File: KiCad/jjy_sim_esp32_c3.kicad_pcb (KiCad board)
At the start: 2 copper layers, 50 x 100 mm, 98 parts, among them J1 UART, J2 BAT, M1 NEJI_M3, M2 NEJI_M3, M3 NEJI_M3, M4 NEJI_M3, P1 USB_C_Plug_USB2.0, Q1 BSS84, Q2 2PD601AR, Q3 HN1C01FU-GR (1/2)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

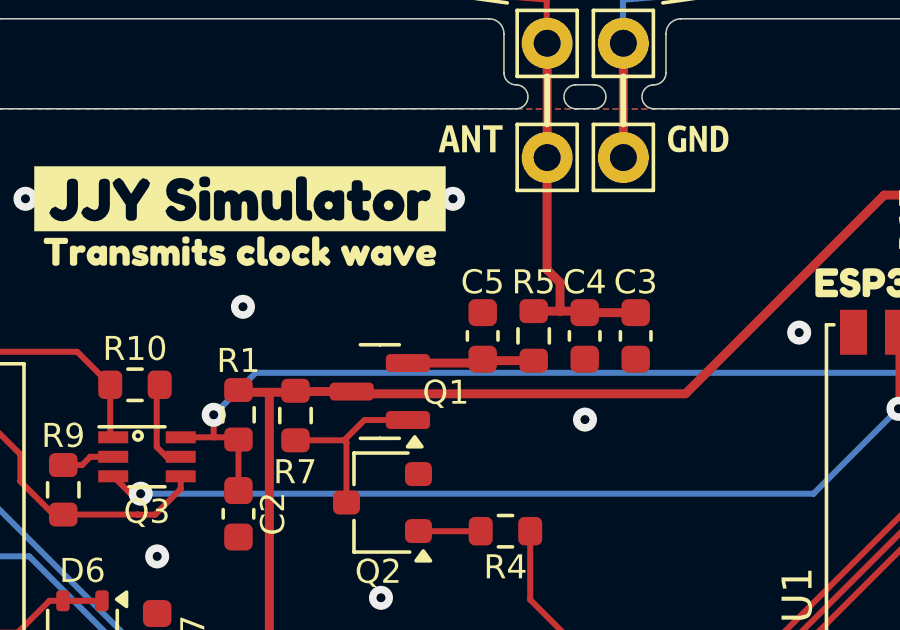
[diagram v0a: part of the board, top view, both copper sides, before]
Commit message: C3,C4定数変更、C5をR18に変更
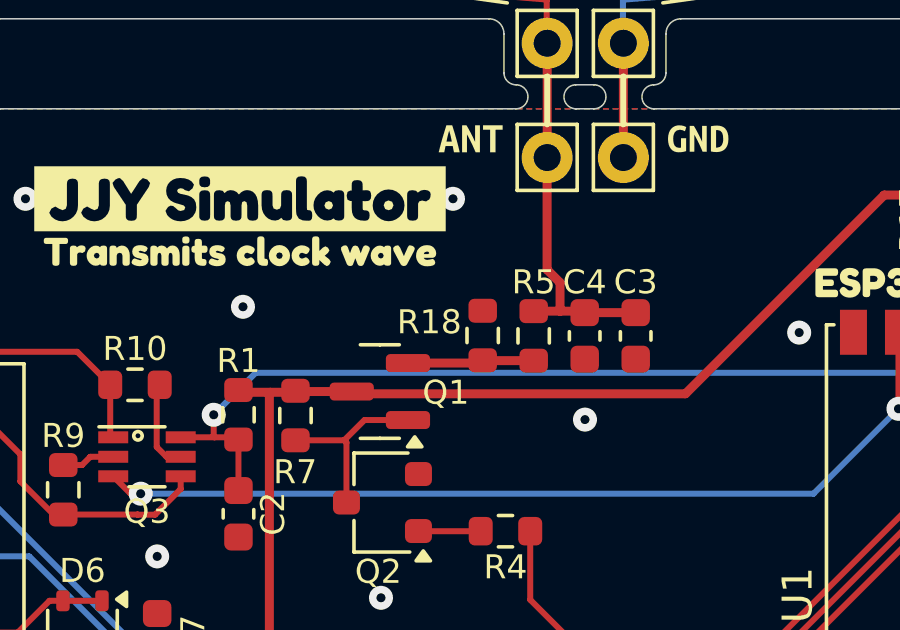
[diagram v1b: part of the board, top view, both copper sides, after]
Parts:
- removed C5: 0.1u, Capacitor_SMD:C_0603_1608Metric
- added R18: 100k, Resistor_SMD:R_0603_1608Metric, F.Cu at (121.6, 107.6)
- C3, C4: value 0.1u -> 1nF
- D2: value LED-IND -> LED-Wave
- D3: value LED-ACT -> LED-WiFi
- D4: value LED-PWR -> LED-Power
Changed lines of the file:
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@@
 			)
 		)
-		(property "Value" "LED-IND"
+		(property "Value" "LED-Wave"
 			(at 0 1.43 180)
 			(layer "F.Fab")
@@
 			)
 		)
-		(property "Value" "0.1u"
+		(property "Value" "1nF"
 			(at 0 1.43 90)
 			(layer "F.Fab")
@@
 		)
 	)
-	(footprint "Capacitor_SMD:C_0603_1608Metric"
-		(layer "F.Cu")
-		(at 121.59 107.57 90)
-		(descr "Capacitor SMD 0603 (1608 Metric), square (rectangular) end terminal, IPC_7351 nominal, (Body size source: IPC-SM-782 page 76, https://www.pcb-3d.com/wordpress/wp-content/uploads/ipc-sm-782a_amendment_1_and_2.pdf), generated with kicad-footprint-generator")
-		(tags "capacitor")
-		(property "Reference" "C5"
-			(at 1.79 0 180)
-			(layer "F.SilkS")
-			(effects
-				(font
-					(size 0.8 0.8)
-					(thickness 0.12)
-				)
-			)
-		)
-		(property "Value" "0.1u"
-			(at 0 1.43 90)
-			(layer "F.Fab")
-			(effects
-				(font
-					(size 0.8 0.8)
-					(thickness 0.12)
-				)
-			)
-		)
-		(property "Footprint" "Capacitor_SMD:C_0603_1608Metric"
-			(at 0 0 90)
-			(unlocked yes)
-			(layer "F.Fab")
-			(hide yes)
-			(effects
-				(font
-					(size 1.27 1.27)
-					(thickness 0.15)
-				)
-			)
-		)
-		(property "Datasheet" ""
-			(at 0 0 90)
-			(unlocked yes)
-			(layer "F.Fab")
-			(hide yes)
-			(effects
-				(font
-					(size 1.27 1.27)
-					(thickness 0.15)
-				)
-			)
-		)
-		(property "Description" ""
-			(at 0 0 90)
-			(unlocked yes)
-			(layer "F.Fab")
-			(hide yes)
-			(effects
-				(font
-					(size 1.27 1.27)
-					(thickness 0.15)
-				)
-			)
-		)
-		(property ki_fp_filters "C_*")
-		(sheetname "ルート")
-		(sheetfile "jjy_sim_esp32_c3.kicad_sch")
-		(attr smd)
-		(fp_line
-			(start -0.14058 -0.51)
-			(end 0.14058 -0.51)
-			(stroke
-				(width 0.12)
-				(type solid)
-			)
-			(layer "F.SilkS")
-		)
-		(fp_line
-			(start -0.14058 0.51)
-			(end 0.14058 0.51)
-			(stroke
-				(width 0.12)
-				(type solid)
-			)
-			(layer "F.SilkS")
-		)
-		(fp_line
-			(start 1.48 -0.73)
-			(end 1.48 0.73)
-			(stroke
-				(width 0.05)
-				(type solid)
-			)
-			(layer "F.CrtYd")
-		)
-		(fp_line
-			(start -1.48 -0.73)
-			(end 1.48 -0.73)
-			(stroke
-				(width 0.05)
-				(type solid)
-			)
-			(layer "F.CrtYd")
-		)
-		(fp_line
-			(start 1.48 0.73)
-			(end -1.48 0.73)
-			(stroke
-				(width 0.05)
-				(type solid)
-			)
-			(layer "F.CrtYd")
-		)
-		(fp_line
-			(start -1.48 0.73)
-			(end -1.48 -0.73)
-			(stroke
-				(width 0.05)
-				(type solid)
-			)
-			(layer "F.CrtYd")
-		)
-		(fp_line
-			(start 0.8 -0.4)
-			(end 0.8 0.4)
-			(stroke
-				(width 0.1)
-				(type solid)
-			)
-			(layer "F.Fab")
-		)
-		(fp_line
-			(start -0.8 -0.4)
-			(end 0.8 -0.4)
-			(stroke
-				(width 0.1)
-				(type solid)
-			)
-			(layer "F.Fab")
-		)
-		(fp_line
-			(start 0.8 0.4)
-			(end -0.8 0.4)
-			(stroke
-				(width 0.1)
-				(type solid)
-			)
-			(layer "F.Fab")
-		)
-		(fp_line
-			(start -0.8 0.4)
-			(end -0.8 -0.4)
-			(stroke
-				(width 0.1)
-				(type solid)
-			)
-			(layer "F.Fab")
-		)
-		(fp_text user "${REFERENCE}"
-			(at 0 0 90)
-			(layer "F.Fab")
-			(effects
-				(font
-					(size 0.4 0.4)
-					(thickness 0.06)
-				)
-			)
-		)
-		(pad "1" smd roundrect
-			(at -0.775 0 90)
-			(size 0.9 0.95)
-			(layers "F.Cu" "F.Paste" "F.Mask")
-			(roundrect_rratio 0.25)
-			(net 5 "Net-(Q1-S)")
-			(pintype "passive")
-		)
-		(pad "2" smd roundrect
-			(at 0.775 0 90)
-			(size 0.9 0.95)
-			(layers "F.Cu" "F.Paste" "F.Mask")
-			(roundrect_rratio 0.25)
-			(net 1 "GND")
-			(pintype "passive")
-		)
-		(model "${KICAD8_3DMODEL_DIR}/Capacitor_SMD.3dshapes/C_0603_1608Metric.wrl"
-			(offset
-				(xyz 0 0 0)
-			)
-			(scale
-				(xyz 1 1 1)
-			)
-			(rotate
-				(xyz 0 0 0)
-			)
-		)
-	)
 	(footprint "kibuzzard-6649687C"
 		(layer "F.Cu")
@@
 			)
 		)
-		(property "Value" "LED-ACT"
+		(property "Value" "LED-WiFi"
 			(at 0 1.43 180)
 			(layer "F.Fab")
@@
 		)
 	)
+	(footprint "Resistor_SMD:R_0603_1608Metric"
+		(layer "F.Cu")
+		(at 121.59 107.557 90)
+		(descr "Resistor SMD 0603 (1608 Metric), square (rectangular) end terminal, IPC_7351 nominal, (Body size source: IPC-SM-782 page 72, https://www.pcb-3d.com/wordpress/wp-content/uploads/ipc-sm-782a_amendment_1_and_2.pdf), generated with kicad-footprint-generator")
+		(tags "resistor")
+		(property "Reference" "R18"
+			(at 0.445 -1.778 180)
+			(layer "F.SilkS")
+			(effects
+				(font
+					(size 0.8 0.8)
+					(thickness 0.12)
+				)
+			)
+		)
+		(property "Value" "100k"
+			(at 0 1.43 90)
+			(layer "F.Fab")
+			(effects
+				(font
+					(size 1 1)
+					(thickness 0.15)
+				)
+			)
+		)
+		(property "Footprint" "Resistor_SMD:R_0603_1608Metric"
+			(at 0 0 90)
+			(unlocked yes)
+			(layer "F.Fab")
+			(hide yes)
+			(effects
+				(font
+					(size 1.27 1.27)
+					(thickness 0.15)
+				)
+			)
+		)
+		(property "Datasheet" ""
+			(at 0 0 90)
+			(unlocked yes)
+			(layer "F.Fab")
+			(hide yes)
+			(effects
+				(font
+					(size 1.27 1.27)
+					(thickness 0.15)
+				)
+			)
+		)
+		(property "Description" ""
+			(at 0 0 90)
+			(unlocked yes)
+			(layer "F.Fab")
+			(hide yes)
+			(effects
+				(font
+					(size 1.27 1.27)
+					(thickness 0.15)
+				)
+			)
+		)
+		(property ki_fp_filters "R_*")
+		(sheetname "ルート")
+		(sheetfile "jjy_sim_esp32_c3.kicad_sch")
+		(attr smd)
+		(fp_line
+			(start -0.237258 -0.5225)
+			(end 0.237258 -0.5225)
+			(stroke
+				(width 0.12)
+				(type solid)
+			)
+			(layer "F.SilkS")
+		)
+		(fp_line
+			(start -0.237258 0.5225)
+			(end 0.237258 0.5225)
+			(stroke
+				(width 0.12)
+				(type solid)
+			)
+			(layer "F.SilkS")
+		)
+		(fp_line
+			(start 1.48 -0.73)
+			(end 1.48 0.73)
+			(stroke
+				(width 0.05)
+				(type solid)
+			)
+			(layer "F.CrtYd")
+		)
+		(fp_line
+			(start -1.48 -0.73)
+			(end 1.48 -0.73)
+			(stroke
+				(width 0.05)
+				(type solid)
+			)
+			(layer "F.CrtYd")
+		)
+		(fp_line
+			(start 1.48 0.73)
+			(end -1.48 0.73)
+			(stroke
+				(width 0.05)
+				(type solid)
+			)
+			(layer "F.CrtYd")
+		)
+		(fp_line
+			(start -1.48 0.73)
+			(end -1.48 -0.73)
+			(stroke
+				(width 0.05)
+				(type solid)
+			)
+			(layer "F.CrtYd")
+		)
+		(fp_line
+			(start 0.8 -0.4125)
+			(end 0.8 0.4125)
+			(stroke
+				(width 0.1)
+				(type solid)
+			)
+			(layer "F.Fab")
+		)
+		(fp_line
+			(start -0.8 -0.4125)
+			(end 0.8 -0.4125)
+			(stroke
+				(width 0.1)
+				(type solid)
+			)
+			(layer "F.Fab")
+		)
+		(fp_line
+			(start 0.8 0.4125)
+			(end -0.8 0.4125)
+			(stroke
+				(width 0.1)
+				(type solid)
+			)
+			(layer "F.Fab")
+		)
+		(fp_line
+			(start -0.8 0.4125)
+			(end -0.8 -0.4125)
+			(stroke
+				(width 0.1)
+				(type solid)
+			)
+			(layer "F.Fab")
+		)
+		(fp_text user "${REFERENCE}"
+			(at 0 0 90)
+			(layer "F.Fab")
+			(effects
+				(font
+					(size 0.4 0.4)
+					(thickness 0.06)
+				)
+			)
+		)
+		(pad "1" smd roundrect
+			(at -0.825 0 90)
+			(size 0.8 0.95)
+			(layers "F.Cu" "F.Paste" "F.Mask")
+			(roundrect_rratio 0.25)
+			(net 5 "Net-(Q1-S)")
+			(pintype "passive")
+		)
+		(pad "2" smd roundrect
+			(at 0.825 0 90)
+			(size 0.8 0.95)
+			(layers "F.Cu" "F.Paste" "F.Mask")
+			(roundrect_rratio 0.25)
+			(net 1 "GND")
+			(pintype "passive")
+		)
+		(model "${KICAD8_3DMODEL_DIR}/Resistor_SMD.3dshapes/R_0603_1608Metric.wrl"
+			(offset
+				(xyz 0 0 0)
+			)
+			(scale
+				(xyz 1 1 1)
+			)
+			(rotate
+				(xyz 0 0 0)
+			)
+		)
+	)
 	(footprint "TestPoint:TestPoint_THTPad_D1.5mm_Drill0.7mm"
 		(layer "F.Cu")
@@
 			)
 		)
-		(property "Value" "LED-PWR"
+		(property "Value" "LED-Power"
 			(at 0 1.43 180)
 			(layer "F.Fab")
@@
 			)
 		)
-		(property "Value" "0.1u"
+		(property "Value" "1nF"
 			(at 0 1.43 90)
 			(layer "F.Fab")
